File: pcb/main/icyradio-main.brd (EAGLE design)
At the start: 167.7 x 111.2 mm, 694 parts, among them CON101 FPC-22P, CON102 FPC-22P, CON1101 2EDG-2P-5MM-H, CON701 4P-SH-TOP, CON801 PCIE-X4-EDGE, J101 RJ45_MAG_LED_1G-TE-1-2301994-0, J701 TRSJACK, J702 TRSJACK, J703 TRSJACK, M701 SPH0641LM4H-1, M702 SPH0641LM4H-1, Q1 AO3400, Q101 AO3400, Q1101 AO3400, Q1102 AO4805, Q1103 AO3400, Q1104 AO4805, Q1105 AO4805, Q1106 AO3400, T501 UWB1-85E, T502 UWB1-85E, T503 UWB1-85E, T504 UWB1-85E, T505 UWB1-85E, T506 UWB1-85E, T507 UWB1-85E, T508 UWB1-85E, U1001 LTC4313-3, U1002 UPD301C, U1003 MIC2019, U101 MIC2019, U102 RPI-CM4, U1101 MCP1804-3302, U1102 LT7182S, U1201 ADM7172ACPZ-5.0, U1202 ADM7171ACPZ-1.3, U1203 ADM7171ACPZ-3.3, U1204 MIC23159, U1205 MIC5166, U1206 ADM7171ACPZ-1.3, U1207 ADM7171ACPZ-3.3, U1208 MIC23159, U1209 MIC23155, U1210 ADP7142AUJZ-3.3, U201 XC7A100TFGG484, U202 SST26VF064B, U301 MT41K256M16TW-125, U302 DSC1203DA3-333M3333, U401 AD9361, U501 MIC2019, U502 MIC2019, U503 MIC2019, U504 MIC2019, U505 ADL5601, U506 ADL5601, U601 8V97003, U701 ADAU1372, U901 DSB321SDA, U902 SI5351C-B-GM

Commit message: Some PCB touches
Signed-off-by: João Silva <jgc3silva@gmail.com>
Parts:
- removed C425: 1nF, Capacitor:CAP0402
- removed D203: LED0603, LED:0603
- removed R1, R11, R2, R8: 10K Ohms, Resistor:RES0402
- removed R10, R14, R4, R5, R6, R7, R9: 22 Ohms, Resistor:RES0402
- removed R406: 1 Ohms, Resistor:RES0402
- added C1014, C421: 1uF, Capacitor:CAP0402
- added C2: 100uF, Capacitor:CAP0805
- added C722: 2.2uF, Capacitor:CAP0402
- added D201: LED0603, LED:0603
- added FB1, FB701: 1uH, Inductor:IND0603
- added R1014, R220, R221, R804, R805: 10K Ohms, Resistor:RES0402
- added R117, R118, R119: 2.2K Ohms, Resistor:RES0402
- added R201, R202: 4.7K Ohms, Resistor:RES0402
- added R222: 1K Ohms, Resistor:RES0402
- added R403: 14.3K Ohms, Resistor:RES0402
- C1: value 1uF -> 100uF; device Capacitor:CAP0402 -> Capacitor:CAP0805
- C1003: value 220pF -> 1uF
- C1004: value 100nF -> 220pF
- C1008, C1010, C1012: value 1uF -> 100nF
- C1009, C1011, C405: value 100nF -> 1uF
- C401: value DNP -> 100nF
- C402: value 1uF -> DNP
- C403: value 1uF -> 10pF
- C404: value 10pF -> 1uF
- C406: value 10nF -> 10uF
- C408, C413, C414, C415, C420: value 1uF -> 10nF
- C410: value 10uF -> 1uF
- C411, C416, C417, C418: value 10nF -> 1uF
- C422, C424: value 1uF -> 1nF
- C423: value 1nF -> 1uF
- C708: value 10uF -> 100nF
- C709: value 100nF -> 10uF
- C712: value 47uF -> 100nF; device Capacitor:CAP0603 -> Capacitor:CAP0402
- C713, C714: value 47uF -> 100uF; device Capacitor:CAP0603 -> Capacitor:CAP0805
- C718: value DNP -> 47uF; device Capacitor:CAP0402 -> Capacitor:CAP0603
- C720: value 2.2uF -> DNP
- D1003: value LED0603 -> B0530W; device LED:0603 -> Generic Diode:SOD-123
- D1004: value B0530W -> LED0603; device Generic Diode:SOD-123 -> LED:0603
- R1003, R1006: value 4.7K Ohms -> 10K Ohms
- R1004: value 90.9K Ohms -> 4.7K Ohms
- R1005: value 10K Ohms -> 90.9K Ohms
- R1007: value 0 Ohms -> 4.7K Ohms
- R1008: value 10K Ohms -> 0 Ohms
- R1009: value TBD Ohms -> 10K Ohms
- R1010: value 1K Ohms -> TBD Ohms
- R1013: value 10K Ohms -> 1K Ohms
- R108: value DNP -> 10K Ohms
- R109: value 1K Ohms -> DNP
- R110: value 0 Ohms -> 1K Ohms
- R111: value 220 Ohms -> 0 Ohms
- R113: value 2.2K Ohms -> 220 Ohms
- R114, R115: value 2.2K Ohms -> 22 Ohms
- R206, R208, R213: value 4.7K Ohms -> 22 Ohms
- R209: value 100 Ohms -> 22 Ohms
- R210: value 4.7K Ohms -> 100 Ohms
- R212: value 2.4K Ohms -> 22 Ohms
- R215: value 4.7K Ohms -> 2.4K Ohms
- R216: value 1K Ohms -> 4.7K Ohms
- R217, R218: value 10K Ohms -> 4.7K Ohms
- R404: value 14.3K Ohms -> 1 Ohms
- moved C1005 92.9 mm to (61.4, 70.1), turned to 270 degrees
- moved R1002 92.2 mm to (153.5, 77.9), turned to 90 degrees
- moved C1004 91.9 mm to (152.6, 81.4), turned to 0 degrees
- moved R205 84.8 mm to (139.2, 38.7)
- moved R208 72.9 mm to (68.7, 53.3)
- moved R111 62.8 mm to (83.9, 30.8)
- moved R1003 59.5 mm to (61.4, 77.3)
- moved R206 52.1 mm to (63.3, 25.3)
- moved R210 48.2 mm to (71.1, 34.0), flipped to the bottom, turned to 0 degrees
- moved R109 47.0 mm to (130.5, 24.0)
- moved R1004 40.9 mm to (120.5, 83.7)
- moved R1006 40.9 mm to (160.3, 96.7), turned to 90 degrees
- moved R802 39.7 mm to (83.5, 19.1), turned to 0 degrees
- moved R1010 37.9 mm to (127.5, 77.8), turned to 180 degrees
- moved R801 37.8 mm to (83.5, 20.1)
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- renumbered JP1 to JP101, Q1 to Q102, R12 to R203, R13 to R204, R3 to R211, S1 to S1001
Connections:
- new net 3V3_CODEC_DIG: C707.1, FB701.1, U701.40
- new net 3V3_DDR3_CLK: C323.1, FB1.2, U302.1, U302.6
- net !CM4_EE_WP: now also R109.2; no longer R108.2
- net !FPGA_FLASH_CS: now also R215.1; no longer R212.1
- net !FPGA_INIT: now also D201.A, R219.1; no longer D202.A, R216.1
- net !FPGA_PROGRAM: now also R214.1; no longer R210.1
- net !PCIE_CM4_CLK_REQ: now also R802.1; no longer R2.1
- net !PCIE_CM4_RST: now also R801.1; no longer R1.1
- net !PCIE_SLOT_CLK_REQ: now also R803.1; no longer R801.1
- net !PCIE_SLOT_RST: now also R805.1; no longer R803.1
- net !PCIE_SLOT_WAKE: now also R804.1; no longer R802.1
- net !PMC_BTN: now also C1003.1, R1002.1; no longer C1.1, R11.1
- net !PMC_RESET: now also R1014.1; no longer R1013.1
- net 1V1_TRX_RX_VCO: now also C423.1; no longer C425.1
- net 1V1_TRX_TX_VCO: now also C421.1; no longer C423.1
- net 1V2: now also R210.2; no longer R209.2
- net 1V3_TRX: now also C404.1, C407.1, C410.1, C413.1, C416.1, C419.1; no longer C402.1, C406.1, C408.1, C411.1, C414.1, C417.1
- net 1V3_TRX_LO_SYNTH: now also C405.1, C408.1, C411.1, C414.1, C417.1, C420.1; no longer C403.1, C407.1, C409.1, C412.1, C415.1, C418.1
- net 2V5: now also C401.1; no longer C405.1
- net 2V5_TRX_INTF_GPO_AUXDAC: now also C406.1, C409.1, C412.1, C415.1, C418.1; no longer C410.1, C413.1, C416.1, C419.1, C420.1
- net 3V3: now also C1005.1, C708.1, FB1.1, FB701.2, R201.2, R202.2, R220.2, R221.2, R222.2, R804.2, R805.2; no longer C1004.1, C323.1, C707.1, R206.2, R208.2, R210.2, R212.2, R216.2, R801.2, R802.2, U302.1, U302.6, U701.40
- net 3V3_CM4: now also R108.2, R117.2, R118.2, R119.2, R801.2, R802.2; no longer R1.2, R111.2, R114.2, R115.2, R2.2, R8.2
- net 3V3_CODEC: now also C712.1; no longer C710.1
- net 3V3_PM: now also C1008.1, C1010.1, R1002.2, R1004.2, R1007.2, R1014.2; no longer C1006.1, C1009.1, R1003.2, R1006.2, R1013.2, R11.2
- net 5V0: now also C1013.1; no longer C1011.1
- net AUDIO_I2C_SCL: now also R207.1; no longer R208.1
- net AUDIO_I2C_SDA: now also R205.1; no longer R207.1
- net CM4_CAM0_SCL: now also R117.1; no longer R114.1
- net CM4_CAM0_SDA: now also R116.1; no longer R113.1
- net CM4_CAM1_SCL: now also R119.1; no longer R116.1
- net CM4_CAM1_SDA: now also R118.1; no longer R115.1
- net CM4_GPIO3: now also R108.1; no longer R8.1
- net CM4_PTP_PPS_IN: now also R111.2; no longer R110.2
- net CM4_PTP_PPS_OUT: now also R110.2; no longer R109.2
- net CM4_UART_RXD: now also R114.2; no longer R9.2
- net CM4_UART_TXD: now also R115.2; no longer R10.2
- net CODEC_CM: now also C710.1; no longer C708.1
- net CODEC_LINE_IN_L: now also C717.1; no longer C716.1
- net CODEC_LINE_IN_R: now also C718.1; no longer C717.1
- net CODEC_MICBIAS0: now also C721.1; no longer C720.1
- net CODEC_MICBIAS1: now also C722.1; no longer C721.1
- net CODEC_MIC_IN_L: now also C715.1; no longer C714.1
- net CODEC_MIC_IN_R: now also C716.1; no longer C715.1
- net CODEC_OUT_L: now also C2.1, C713.1; no longer C712.1
- net CODEC_OUT_R: now also C1.1, C714.1; no longer C713.1
- net ETH_SYNC_IN: now also R111.1; no longer R110.1
- net ETH_SYNC_OUT: now also R110.1; no longer R109.1
- net EXT_IO_1_2: now also R208.2; no longer R4.2
- net EXT_IO_1_3: now also R212.2; no longer R5.2
- net EXT_IO_1_4: now also R209.2; no longer R6.2
- net EXT_IO_1_5: now also R213.2; no longer R7.2
- net EXT_IO_2_6: now also R206.2; no longer R14.2
- net FPGA_DONE: now also D202.A, R222.1; no longer D203.A, R219.1
- net FPGA_FLASH_IO2: now also R217.1; no longer R214.1
- net FPGA_FLASH_IO3: now also R218.1; no longer R215.1
- net FPGA_JTAG_EN: now also R216.2; no longer R213.2
- net FPGA_TDI: now also R220.1; no longer R217.1
- net FPGA_TMS: now also R221.1; no longer R218.1
- net GND: now also C1014.2, C404.2, C422.2, C424.2, C712.2, C722.2, CON801.A20, CON801.A23, CON801.A24, CON801.A27, CON801.A28, CON801.A31, CON801.B21, CON801.B22, CON801.B25, CON801.B26, CON801.B29, CON801.B32, D1004.C, D201.C, R1003.1, R1006.1, R1010.1, R109.1, R216.1, R403.1; no longer C1.2, C403.2, C423.2, C425.2, C718.2, D1003.C, D203.C, R1002.1, R1005.1, R1008.1, R108.1, R213.1, R406.1
- net N$12: now also C421.2, R404.2; no longer C422.2, R405.2
- net N$19: now also D1004.A, R1013.1; no longer D1003.A, R1010.1
- net N$2: now also R114.1; no longer R9.1
- net N$29: now also C423.2, R405.2; no longer C424.2, R406.2
- net N$31: now also R210.1; no longer R209.1
- net N$32: now also C1009.1; no longer C1008.1
- net N$35: now also R213.1; no longer R7.1
- net N$37: now also R206.1; no longer R14.1
- net N$38: now also C716.2; no longer C715.2
- net N$39: now also C715.2; no longer C714.2
- net N$41: now also R209.1; no longer R6.1
- net N$42: now also C1.2, C714.2; no longer C713.2
- net N$43: now also R212.1; no longer R5.1
- net N$44: now also C2.2, C713.2; no longer C712.2
- net N$45: now also R208.1; no longer R4.1
- net N$48: now also R113.1; no longer R112.1
- net N$50: now also R112.1; no longer R111.1
- net N$55: now also C719.1; no longer C718.1
- net N$56: now also C720.1; no longer C719.1
- net N$6: now also R115.1; no longer R10.1
- net N$7: now also C718.2; no longer C717.2
- net N$8: now also R403.2; no longer R404.2
- net N$9: now also C717.2; no longer C716.2
- net N$93: now also C1011.1; no longer C1010.1
- net N$94: now also C1014.1, D1003.A; no longer C1013.1, D1004.A
- net N$95: now also R1010.2; no longer R1009.2
- net PMC_LED: now also R1013.2; no longer R1010.2
- net PM_I2C_EN: now also R1003.2; no longer R1002.2
- net PM_I2C_SCL: now also R1004.1; no longer R1003.1
- net PM_I2C_SDA: now also R1007.1; no longer R1006.1
- net PM_SPI_MOSI: now also R1008.1; no longer R1007.1
- net PM_SPI_MOSI_SI: now also R1008.2; no longer R1007.2
- net SYS_I2C_SCL: now also R202.1; no longer R206.1
- net SYS_I2C_SDA: now also R201.1; no longer R205.1
- net TRX_REF_CLK_DIV: now also C402.1, C403.1; no longer C401.1, C404.1
- net TRX_XTALN: now also C403.2; no longer C404.2
- net USB_CC2: now also C1004.1; no longer C1003.1
- net USB_VBUS_DET: now also C1006.1, R1005.1, R1006.2; no longer C1005.1, R1004.1, R1005.2
- net VBUS: now also D1003.C, R1005.2; no longer D1004.C, R1004.2
- net VBUS_SRC_EN: now also R1009.2; no longer R1008.2
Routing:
- net GND: track 323.0 -> 355.8 mm, vias 837 -> 1436
- net 3V3_DDR3_CLK: track 0.00 -> 3.91 mm
- net 3V3: track 224.8 -> 221.4 mm
- net 3V3_CODEC_DIG: track 0.00 -> 3.27 mm
- net N$44: track 2.70 -> 4.85 mm
- net N$42: track 2.70 -> 4.85 mm
- net CODEC_OUT_L: track 13.1 -> 14.3 mm
- net !PCIE_SLOT_PRSNT: track 44.0 -> 45.2 mm
- net CODEC_OUT_R: track 13.8 -> 15.0 mm

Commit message: Minor updates
Signed-off-by: João Silva <jgc3silva@gmail.com>
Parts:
- added C3, C4: 47uF, Capacitor:CAP0603
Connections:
- net 2V5: now also C4.1
- net 5V0: now also C3.1
- net GND: now also C3.2, C4.2
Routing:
- net GND: vias 1436 -> 1457

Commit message: Silk screen done
Signed-off-by: João Silva <jgc3silva@gmail.com>
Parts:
- removed C1, C2: 100uF, Capacitor:CAP0805
- removed C3, C4: 47uF, Capacitor:CAP0603
- added C1258: 4.7uF, Capacitor:CAP0603
- added C1259: 10uF, Capacitor:CAP0402
- added C723, C724: 2.2uF, Capacitor:CAP0402
- C1222: value 4.7uF -> 47uF; device Capacitor:CAP0402 -> Capacitor:CAP0603
- C1223: value 1uF -> 47uF; device Capacitor:CAP0402 -> Capacitor:CAP0603
- C1224: value 100nF -> 4.7uF
- C1225: value 100uF -> 1uF; device Capacitor:CAP1206 -> Capacitor:CAP0402
- C1227, C1254: value 100nF -> 100uF; device Capacitor:CAP0402 -> Capacitor:CAP1206
- C1229: value 10nF -> 100nF
- C1230, C1256: value 4.7uF -> 100nF; device Capacitor:CAP0603 -> Capacitor:CAP0402
- C1232: value 1uF -> 4.7uF; device Capacitor:CAP0402 -> Capacitor:CAP0603
- C1233: value 10uF -> 10nF
- C1234: value 10uF -> 1uF
- C1237, C1243: value 100nF -> 10uF
- C1239, C1253: value 10uF -> 100nF
- C1240: value 4.7uF -> 10uF; device Capacitor:CAP0603 -> Capacitor:CAP0402
- C1242: value 10uF -> 4.7uF; device Capacitor:CAP0402 -> Capacitor:CAP0603
- C1244: value 100uF -> 10uF; device Capacitor:CAP1206 -> Capacitor:CAP0402
- C1246: value 4.7uF -> 100uF; device Capacitor:CAP0603 -> Capacitor:CAP1206
- C1247, C1250: value 470pF -> 100nF
- C1248: value 100nF -> 4.7uF; device Capacitor:CAP0402 -> Capacitor:CAP0603
- C1251: value 100nF -> 470pF
- C1252: value 100uF -> 470pF; device Capacitor:CAP1206 -> Capacitor:CAP0402
- C712: value 100nF -> 100uF; device Capacitor:CAP0402 -> Capacitor:CAP0805
- C715: value 47uF -> 100uF; device Capacitor:CAP0603 -> Capacitor:CAP0805
- C716: value 47uF -> 100nF; device Capacitor:CAP0603 -> Capacitor:CAP0402
- C719, C720: value DNP -> 47uF; device Capacitor:CAP0402 -> Capacitor:CAP0603
- C721, C722: value 2.2uF -> DNP
- moved C1236 85.5 mm to (28.5, 68.8), turned to 180 degrees
- moved C1238 85.4 mm to (113.2, 57.1), turned to 0 degrees
- moved C1226 85.2 mm to (114.5, 68.4), turned to 90 degrees
- moved C1222 81.3 mm to (27.3, 75.1), turned to 90 degrees
- moved C1234 78.7 mm to (106.6, 59.1)
- moved C1228 77.4 mm to (29.5, 74.6), turned to 0 degrees
- moved C1243 65.1 mm to (28.5, 66.8), turned to 180 degrees
- moved C1235 64.7 mm to (113.2, 58.1), turned to 0 degrees
- moved C1240 64.2 mm to (28.5, 67.8)
- moved C1233 63.9 mm to (57.2, 88.8), turned to 180 degrees
- moved C1244 62.9 mm to (30.5, 66.8)
- moved C1242 62.7 mm to (88.4, 90.8), turned to 180 degrees
- moved C1227 56.5 mm to (113.0, 63.0), turned to 180 degrees
- moved C1250 55.7 mm to (130.2, 52.6), turned to 270 degrees
- moved C1223 52.8 mm to (64.8, 90.4), turned to 270 degrees
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- renumbered FB1 to FB301
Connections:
- net 0V675_DDR3_VREF: now also C1234.1; no longer C1232.1
- net 0V675_DDR3_VTT: now also C1235.1, C1238.1; no longer C1233.1, C1236.1
- net 1V2: now also C1259.1; no longer C1255.1
- net 1V2_SS: now also C1251.1; no longer C1249.1
- net 1V35: now also C1224.1; no longer C1222.1
- net 1V3_TRX: now also C1236.1, C1240.1, C1243.1, C1244.1; no longer C1234.1, C1238.1, C1241.1, C1242.1
- net 1V8: now also C1226.1, C1227.1; no longer C1224.1, C1225.1
- net 2V5: now also C1222.1, C1228.1, C1245.1, C1246.1; no longer C1226.1, C1243.1, C1244.1, C4.1
- net 2V5_SS: now also C1249.1; no longer C1247.1
- net 3V3: now also C1253.1, C1254.1; no longer C1251.1, C1252.1
- net 3V3_CODEC: now also C1255.1, C716.1; no longer C1253.1, C712.1
- net 3V3_SS: now also C1252.1; no longer C1250.1
- net 3V3_SYNTH_VCO_RF: now also C1237.1, C1241.1; no longer C1235.1, C1239.1
- net 5V0: now also C1225.1, C1229.1, C1232.1, C1239.1, C1242.1, C1247.1, C1250.1, C1258.1; no longer C1227.1, C1228.1, C1237.1, C1240.1, C1245.1, C1246.1, C1254.1, C3.1
- net CODEC_LINE_IN_L: now also C719.1; no longer C717.1
- net CODEC_LINE_IN_R: now also C720.1; no longer C718.1
- net CODEC_MICBIAS0: now also C723.1; no longer C721.1
- net CODEC_MICBIAS1: now also C724.1; no longer C722.1
- net CODEC_MIC_IN_L: now also C717.1; no longer C715.1
- net CODEC_MIC_IN_R: now also C718.1; no longer C716.1
- net CODEC_OUT_L: now also C712.1; no longer C2.1
- net CODEC_OUT_R: now also C715.1; no longer C1.1
- net GND: now also C1258.2, C1259.2, C716.2, C723.2, C724.2; no longer C3.2, C4.2, C712.2, C719.2, C720.2
- net N$38: now also C718.2; no longer C716.2
- net N$39: now also C717.2; no longer C715.2
- net N$42: now also C715.2; no longer C1.2
- net N$44: now also C712.2; no longer C2.2
- net N$5: now also C1231.1; no longer C1229.1
- net N$55: now also C721.1; no longer C719.1
- net N$56: now also C722.1; no longer C720.1
- net N$7: now also C720.2; no longer C718.2
- net N$9: now also C719.2; no longer C717.2
- net N$97: now also C1233.1; no longer C1231.1

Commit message: Minor updates
Signed-off-by: João Silva <jgc3silva@gmail.com>
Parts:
- added C909: 100nF, Capacitor:CAP0402
- C615, C903: value 100nF -> 1uF
- C621, C622: value 10nF -> 10pF
- C623, C624, C625, C626: value 100nF -> 20pF
- C905: value 10pF -> 100nF
- C907: value 100nF -> 10pF
- moved C905 9.92 mm to (57.1, 15.5), turned to 180 degrees
- moved C908 9.10 mm to (59.8, 20.6), turned to 90 degrees
- moved C903 8.34 mm to (57.1, 19.4), turned to 180 degrees
- moved C907 7.72 mm to (65.0, 14.9)
- moved C904 5.34 mm to (61.3, 12.2), turned to 270 degrees
- moved C906 2.00 mm to (67.0, 14.9)
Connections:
- net 3V3_CLK_MNGR: now also C905.1, C909.1; no longer C907.1
- net CLK_MNGR_REF_ACC: now also C907.2; no longer C906.2
- net CLK_MNGR_REF_DCC: now also C907.1; no longer C905.1
- net GND: now also C906.2, C909.2; no longer C907.2
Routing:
- net 3V3_CLK_MNGR: track 20.2 -> 21.1 mm
- net GND: vias 1457 -> 1458

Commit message: Minor changes
Signed-off-by: João Silva <jgc3silva@gmail.com>
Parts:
- added C333, C334: 47uF, Capacitor:CAP0603
- C323: value 1uF -> 10uF; device Capacitor:CAP0402 -> Capacitor:CAP0603
- C324: value 100nF -> 1uF
- C325: value 100nF -> 10nF
- C329, C330: value 4.7uF -> 100nF
- C331, C332: value 47uF -> 4.7uF; device Capacitor:CAP0603 -> Capacitor:CAP0402
- R325: value 40.2 Ohms -> DNP
- moved C324 40.6 mm to (83.9, 31.2), turned to 0 degrees
- moved C325 40.2 mm to (83.9, 32.2), turned to 0 degrees
- moved C331 19.3 mm to (92.7, 70.4), turned to 0 degrees
- moved C332 18.3 mm to (85.1, 78.7)
- moved C327 18.2 mm to (74.6, 71.3), turned to 180 degrees
- moved C326 18.2 mm to (68.0, 68.6), turned to 90 degrees
- moved C328 14.1 mm to (83.1, 78.7), turned to 180 degrees
- moved C330 12.8 mm to (92.7, 68.4)
- moved C323 3.64 mm to (87.0, 34.1), turned to 270 degrees
- moved C329 1.00 mm to (92.7, 69.4)
- moved R110 0.60 mm to (83.9, 29.2)
- moved R111 0.60 mm to (83.9, 30.2)
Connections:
- net 0V675_DDR3_VTT: now also C326.2, C333.1, C334.1; no longer C324.2, C325.1, C326.1
- net 3V3: now also C323.1
- net 3V3_DDR3_CLK: now also C324.1, C325.1; no longer C323.1
- net GND: now also C324.2, C333.2, C334.2; no longer C326.2
- net N$87: now also C326.1; no longer C324.1
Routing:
- net 3V3: track 221.3 -> 222.8 mm, vias 42 -> 43
- net 3V3_DDR3_CLK: track 3.91 -> 4.91 mm
- net ETH_SYNC_OUT: track 51.2 -> 50.6 mm
- net GND: vias 1458 -> 1461

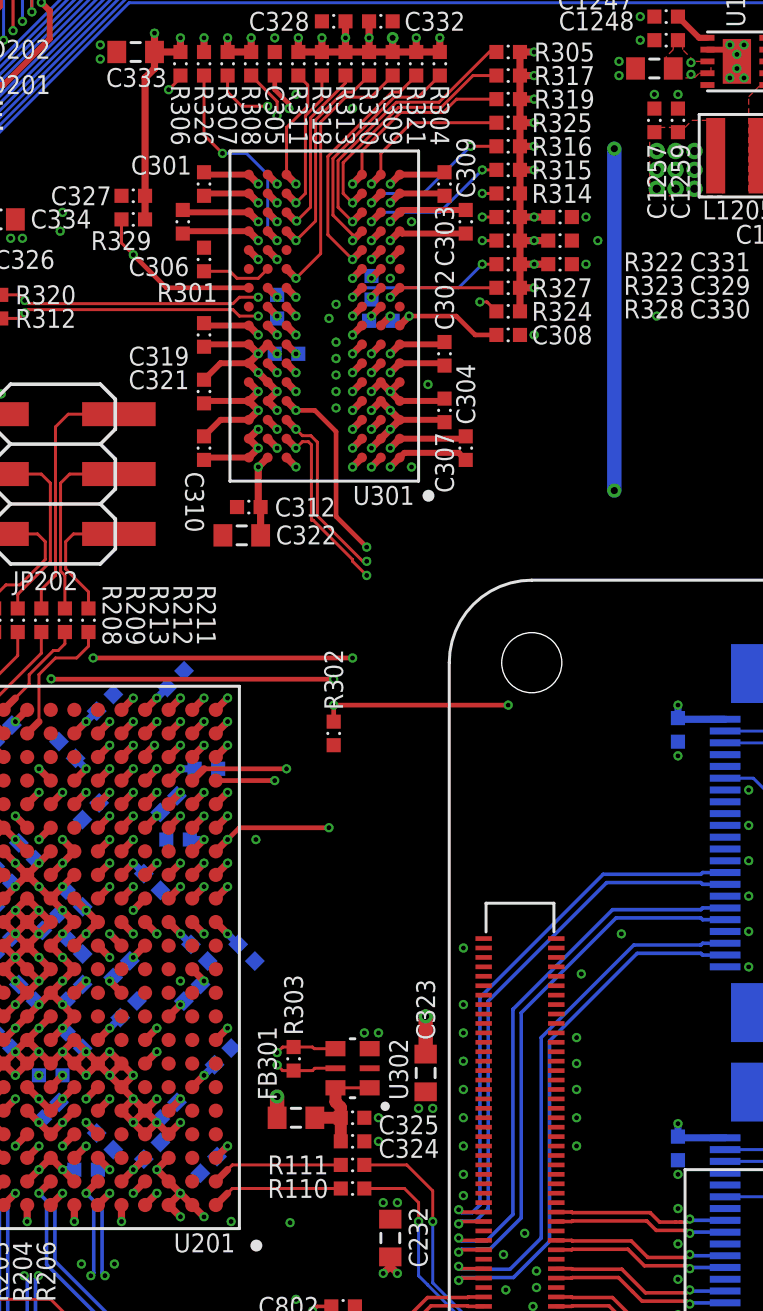
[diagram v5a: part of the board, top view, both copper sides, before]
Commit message: Remove dedicated DDR3 oscillator
Signed-off-by: João Silva <jgc3silva@gmail.com>
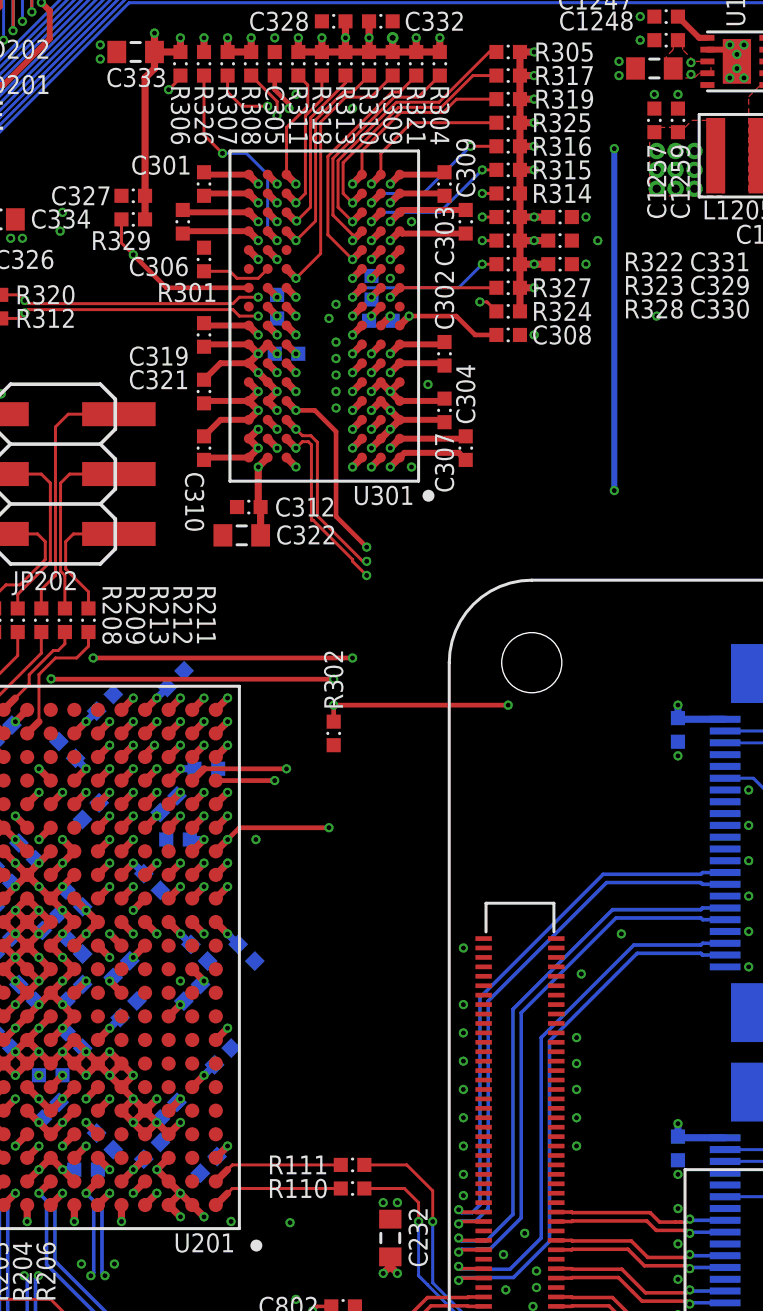
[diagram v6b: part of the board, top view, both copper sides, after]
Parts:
- removed C323: 10uF, Capacitor:CAP0603
- removed C324: 1uF, Capacitor:CAP0402
- removed C325: 10nF, Capacitor:CAP0402
- removed FB301: 1uH, Inductor:IND0603
- removed R303: 100 Ohms, Resistor:RES0402
- removed U302: DSC1203DA3-333M3333, Microchip:VDFN6
- C708: value 100nF -> 1uF
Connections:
- removed net 3V3_DDR3_CLK: C324.1, C325.1, FB301.2, U302.1, U302.6
- removed net DDR3_CLK_IN_N: R303.1, U201.G4, U302.5
- removed net DDR3_CLK_IN_P: R303.2, U201.H4, U302.4
- net 3V3: no longer C323.1, FB301.1
- net GND: no longer C323.2, C324.2, C325.2, U302.3
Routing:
- net 3V3: track 222.8 -> 187.0 mm, vias 43 -> 41
- net DDR3_CLK_IN_N: track 8.96 -> 0.00 mm, vias 2 -> 0
- net DDR3_CLK_IN_P: track 8.95 -> 0.00 mm, vias 2 -> 0
- net 3V3_DDR3_CLK: track 4.91 -> 0.00 mm
- net GND: vias 1461 -> 1455

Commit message: Finish checklist and generate gerbers
Signed-off-by: João Silva <jgc3silva@gmail.com>
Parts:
- removed C332: 4.7uF, Capacitor:CAP0402
- removed C333, C334: 47uF, Capacitor:CAP0603
- removed R329: 40.2 Ohms, Resistor:RES0402
- added C323, C324, C325: 100nF, Capacitor:CAP0402
- added R120, R121: 2.2K Ohms, Resistor:RES0402
- added R303: 40.2 Ohms, Resistor:RES0402
- C328, C329: value 100nF -> 4.7uF
- C330: value 100nF -> 47uF; device Capacitor:CAP0402 -> Capacitor:CAP0603
- C331: value 4.7uF -> 47uF; device Capacitor:CAP0402 -> Capacitor:CAP0603
- R110: value 1K Ohms -> DNP
- R112: value 220 Ohms -> DNP
- R113: value 220 Ohms -> 1K Ohms
- R118, R119: value 2.2K Ohms -> 220 Ohms
- R324: value 40.2 Ohms -> DNP
- R325: value DNP -> 40.2 Ohms
- moved R113 65.6 mm to (83.9, 30.1)
- moved R112 62.6 mm to (83.9, 29.1)
- moved C326 24.7 mm to (92.7, 69.4), turned to 0 degrees
- moved C331 23.9 mm to (68.8, 70.3)
- moved R319 23.5 mm to (68.5, 67.1)
- moved R119 22.8 mm to (146.2, 9.40), turned to 180 degrees
- moved R320 20.6 mm to (86.6, 76.9), turned to 90 degrees
- moved C330 20.1 mm to (74.7, 77.4), turned to 180 degrees
- moved R312 18.6 mm to (83.6, 76.9), turned to 270 degrees
- moved C327 18.3 mm to (92.7, 68.4), turned to 0 degrees
- moved R311 17.0 mm to (68.5, 66.1), turned to 0 degrees
- moved R326 16.0 mm to (90.5, 67.4), turned to 0 degrees
- moved R328 16.0 mm to (74.6, 70.3)
- moved R118 15.9 mm to (146.2, 22.6), turned to 180 degrees
- moved R305 13.9 mm to (76.6, 76.9), turned to 270 degrees
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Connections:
- net !DDR3_CAS: now also R327.1; no longer R328.1
- net !DDR3_RAS: now also R323.1; no longer R324.1
- net !DDR3_RESET: now also R324.1; no longer R325.1
- net !DDR3_WE: now also R322.1; no longer R323.1
- net 0V675_DDR3_VTT: now also C323.2, C324.1, C325.1, C326.1, R303.1, R312.1, R320.2; no longer C326.2, C332.1, C333.1, C334.1, R311.1, R319.1, R329.2
- net 3V3_CM4: now also R120.2, R121.2; no longer R112.2, R113.2
- net CM4_CAM1_SCL: now also R121.1; no longer R119.1
- net CM4_CAM1_SDA: now also R120.1; no longer R118.1
- net CM4_PTP_PPS_IN: now also R110.2
- net CM4_PTP_PPS_OUT: now also R112.2, R113.2; no longer R110.2
- net DDR3_A0: now also R303.2; no longer R304.2
- net DDR3_A1: now also R312.2; no longer R313.2
- net DDR3_A10: now also R308.2; no longer R309.2
- net DDR3_A11: now also R317.2; no longer R318.2
- net DDR3_A12: now also R309.2; no longer R310.2
- net DDR3_A13: now also R318.2; no longer R319.2
- net DDR3_A14: now also R310.2; no longer R311.2
- net DDR3_A2: now also R304.2; no longer R305.2
- net DDR3_A3: now also R313.2; no longer R314.2
- net DDR3_A4: now also R305.2; no longer R306.2
- net DDR3_A5: now also R314.2; no longer R315.2
- net DDR3_A6: now also R306.2; no longer R307.2
- net DDR3_A7: now also R315.2; no longer R316.2
- net DDR3_A8: now also R307.2; no longer R308.2
- net DDR3_A9: now also R316.2; no longer R317.2
- net DDR3_BA0: now also R321.1; no longer R322.1
- net DDR3_BA1: now also R325.1; no longer R326.1
- net DDR3_BA2: now also R320.1; no longer R321.1
- net DDR3_CLK_EN: now also R328.1; no longer R329.1
- net DDR3_CLK_N: now also R319.1; no longer R320.1
- net DDR3_CLK_P: now also R311.2; no longer R312.2
- net DDR3_ODT: now also R326.1; no longer R327.1
- net ETH_SYNC_OUT: now also R113.1; no longer R110.1
- net GND: now also C324.2, C325.2, C326.2, R110.1, R112.1, U401.L5; no longer C332.2, C333.2, C334.2
- net N$48: now also R119.1; no longer R113.1
- net N$50: now also R118.1; no longer R112.1
- net N$87: now also C323.1, R311.1, R319.2; no longer C326.1, R312.1, R320.2
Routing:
- net GND: track 355.8 -> 360.0 mm, vias 1455 -> 1475
- net CM4_PTP_PPS_OUT: track 5.59 -> 6.96 mm
- net CM4_PTP_PPS_IN: track 5.59 -> 6.96 mm
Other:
- board text added: "IcyRadio v2 Sep 2023"
- board text removed: "IcyRadio v2 Jan 2023"
